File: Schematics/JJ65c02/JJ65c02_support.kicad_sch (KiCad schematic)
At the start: 37 parts, among them J1 AudioJack, SW2 SW_SPDT, U10 VIA Port Shifter, U11 Misc Shifter, U5 TLV2217-33KCSE3, U9 Data Level Shifter, X1 4Mhz, X2 1.8Mhz

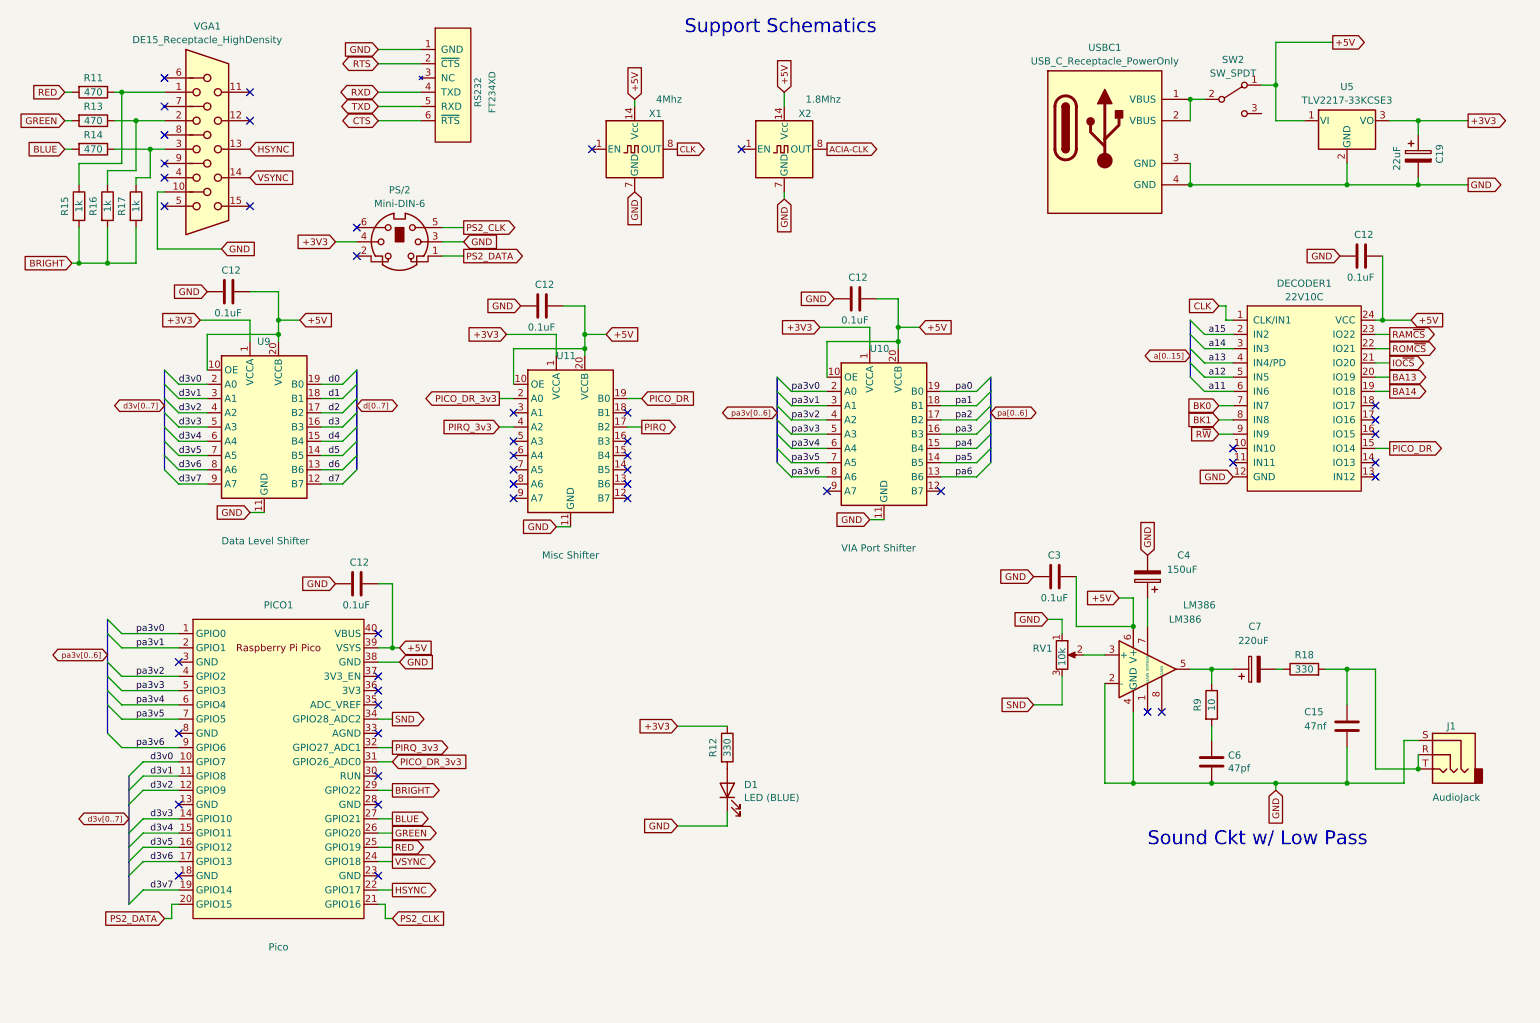
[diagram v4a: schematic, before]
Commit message: Updated schematics for v2-pico
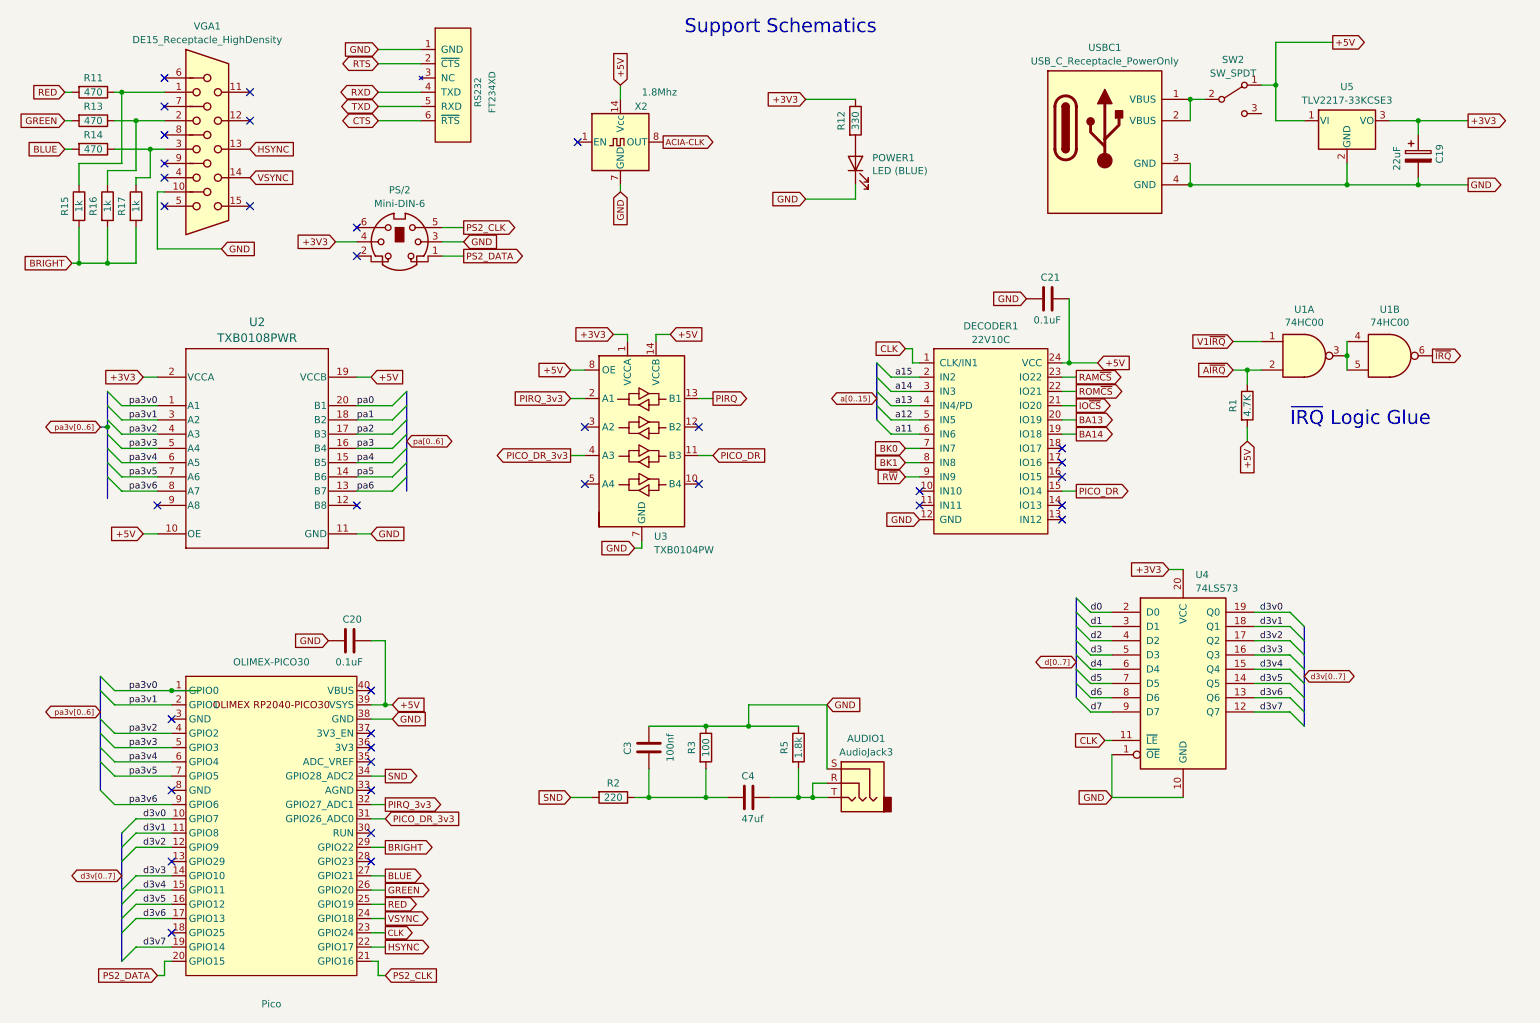
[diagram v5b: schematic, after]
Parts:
- removed C12 (x3): 0.1uF, Capacitor_THT:C_Disc_D4.7mm_W2.5mm_P5.00mm, symbol Device:C
- removed C15: 47nf, Capacitor_THT:C_Disc_D4.7mm_W2.5mm_P5.00mm, symbol Device:C
- removed C4: 150uF, Capacitor_THT:CP_Radial_D5.0mm_P2.50mm, symbol Device:C_Polarized
- removed C6: 47pf, Capacitor_THT:C_Disc_D4.7mm_W2.5mm_P5.00mm, symbol Device:C
- removed C7: 220uF, Capacitor_THT:CP_Radial_D6.3mm_P2.50mm, symbol Device:C_Polarized
- removed J1: AudioJack, Connector_Audio:Jack_3.5mm_CUI_SJ1-3533NG_Horizontal, symbol Connector:AudioJack3
- removed LM386: LM386, Package_DIP:DIP-8_W7.62mm_Socket, symbol Amplifier_Audio:LM386
- removed R18: 330, Resistor_THT:R_Axial_DIN0207_L6.3mm_D2.5mm_P7.62mm_Horizontal, symbol Device:R
- removed R9: 10, Resistor_THT:R_Axial_DIN0207_L6.3mm_D2.5mm_P7.62mm_Horizontal, symbol Device:R
- removed RV1: 10k, Potentiometer_THT:Potentiometer_Bourns_3339P_Vertical, symbol Device:R_Potentiometer
- removed U10: VIA Port Shifter, JJ65c02:TXB0108, symbol JJ65c02-rescue:FXMA108
- removed U11: Misc Shifter, JJ65c02:TXB0108, symbol JJ65c02-rescue:FXMA108
- removed U9: Data Level Shifter, JJ65c02:TXB0108, symbol JJ65c02-rescue:FXMA108
- removed X1: 4Mhz, Oscillator:Oscillator_DIP-14, symbol Oscillator:CXO_DIP14
- added AUDIO1: AudioJack3, Connector_Audio:Jack_3.5mm_CUI_SJ1-3533NG_Horizontal, symbol Connector_Audio:AudioJack3
- added C4: 47uf, Capacitor_THT:C_Disc_D4.7mm_W2.5mm_P5.00mm, symbol Device:C
- added R1: 4.7K, Resistor_THT:R_Axial_DIN0207_L6.3mm_D2.5mm_P7.62mm_Horizontal, symbol Device:R
- added R2: 220, Resistor_THT:R_Axial_DIN0207_L6.3mm_D2.5mm_P7.62mm_Horizontal, symbol Device:R
- added R3: 100, Resistor_THT:R_Axial_DIN0207_L6.3mm_D2.5mm_P7.62mm_Horizontal, symbol Device:R
- added R5: 1.8k, Resistor_THT:R_Axial_DIN0207_L6.3mm_D2.5mm_P7.62mm_Horizontal, symbol Device:R
- added U1: 74HC00, Package_DIP:DIP-14_W7.62mm_Socket, symbol 74xx:74HC00
- added U2: TXB0108PWR, Package_SO:TSSOP-20_4.4x6.5mm_P0.65mm, symbol 2024-01-03_21-33-35:TXB0108PWR
- added U3: TXB0104PW, Package_SO:SOIC-14_3.9x8.7mm_P1.27mm, symbol Logic_LevelTranslator:TXB0104PW
- added U4: 74LS573, Package_SO:SOIC-20W_7.5x12.8mm_P1.27mm, symbol 74xx:74LS573
- C3: value 0.1uF -> 100nf
- renumbered C12 to C20, C12 to C21, PICO1 to OLIMEX-PICO30, D1 to POWER1
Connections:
- net +3V3: now also U2.2 (VCCA), U3.1 (VCCA), U4.20 (VCC)
- net +5V: now also R1.2, U2.10 (OE), U2.19 (VCCB), U3.14 (VCCB), U3.8 (OE); no longer C3.1
- net CLK: now also OLIMEX-PICO30.23 (GPIO24), U4.11 (~{LE})
- net GND: now also C3.1, AUDIO1.S, R3.1, R5.1, U2.11 (GND), U3.7 (GND), U4.1 (~{OE}), U4.10 (GND); no longer C3.2
- net PICO_DR: now also U3.11 (B3)
- net PICO_DR_3v3: now also U3.4 (A3)
- net PIRQ: now also U3.13 (B1)
- net PIRQ_3v3: now also U3.2 (A1)
- net SND: now also R2.2
- net d0: now also U4.2 (D0)
- net d1: now also U4.3 (D1)
- net d2: now also U4.4 (D2)
- net d3: now also U4.5 (D3)
- net d3v0: now also U4.19 (Q0)
- net d3v1: now also U4.18 (Q1)
- net d3v2: now also U4.17 (Q2)
- net d3v3: now also U4.16 (Q3)
- net d3v4: now also U4.15 (Q4)
- net d3v5: now also U4.14 (Q5)
- net d3v6: now also U4.13 (Q6)
- net d3v7: now also U4.12 (Q7)
- net d4: now also U4.6 (D4)
- net d5: now also U4.7 (D5)
- net d6: now also U4.8 (D6)
- net d7: now also U4.9 (D7)
- net pa0: now also U2.20 (B1)
- net pa1: now also U2.18 (B2)
- net pa2: now also U2.17 (B3)
- net pa3: now also U2.16 (B4)
- net pa3v0: now also U2.1 (A1)
- net pa3v1: now also U2.3 (A2)
- net pa3v2: now also U2.4 (A3)
- net pa3v3: now also U2.5 (A4)
- net pa3v4: now also U2.6 (A5)
- net pa3v5: now also U2.7 (A6)
- net pa3v6: now also U2.8 (A7)
- net pa4: now also U2.15 (B5)
- net pa5: now also U2.14 (B6)
- net pa6: now also U2.13 (B7)
- new net: C3.2, C4.2, R2.1, R3.2
- new net: U1.3, U1.4, U1.5
- new net: AUDIO1.R, AUDIO1.T, C4.1, R5.2
- new net A~{IRQ}: R1.1, U1.2
- new net V1~{IRQ}: U1.1
- new net ~{IRQ}: U1.6
- no-connect marks 48 -> 36
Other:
- note added: "~{IRQ} Logic Glue"
- note removed: "Sound Ckt w/ Low Pass"
- moved on the sheet: C20, C21, DECODER1, OLIMEX-PICO30, POWER1, R12, X2

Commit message: if we are using the pi pico to generate the clock, we need to level convert from 3.3 to 5v
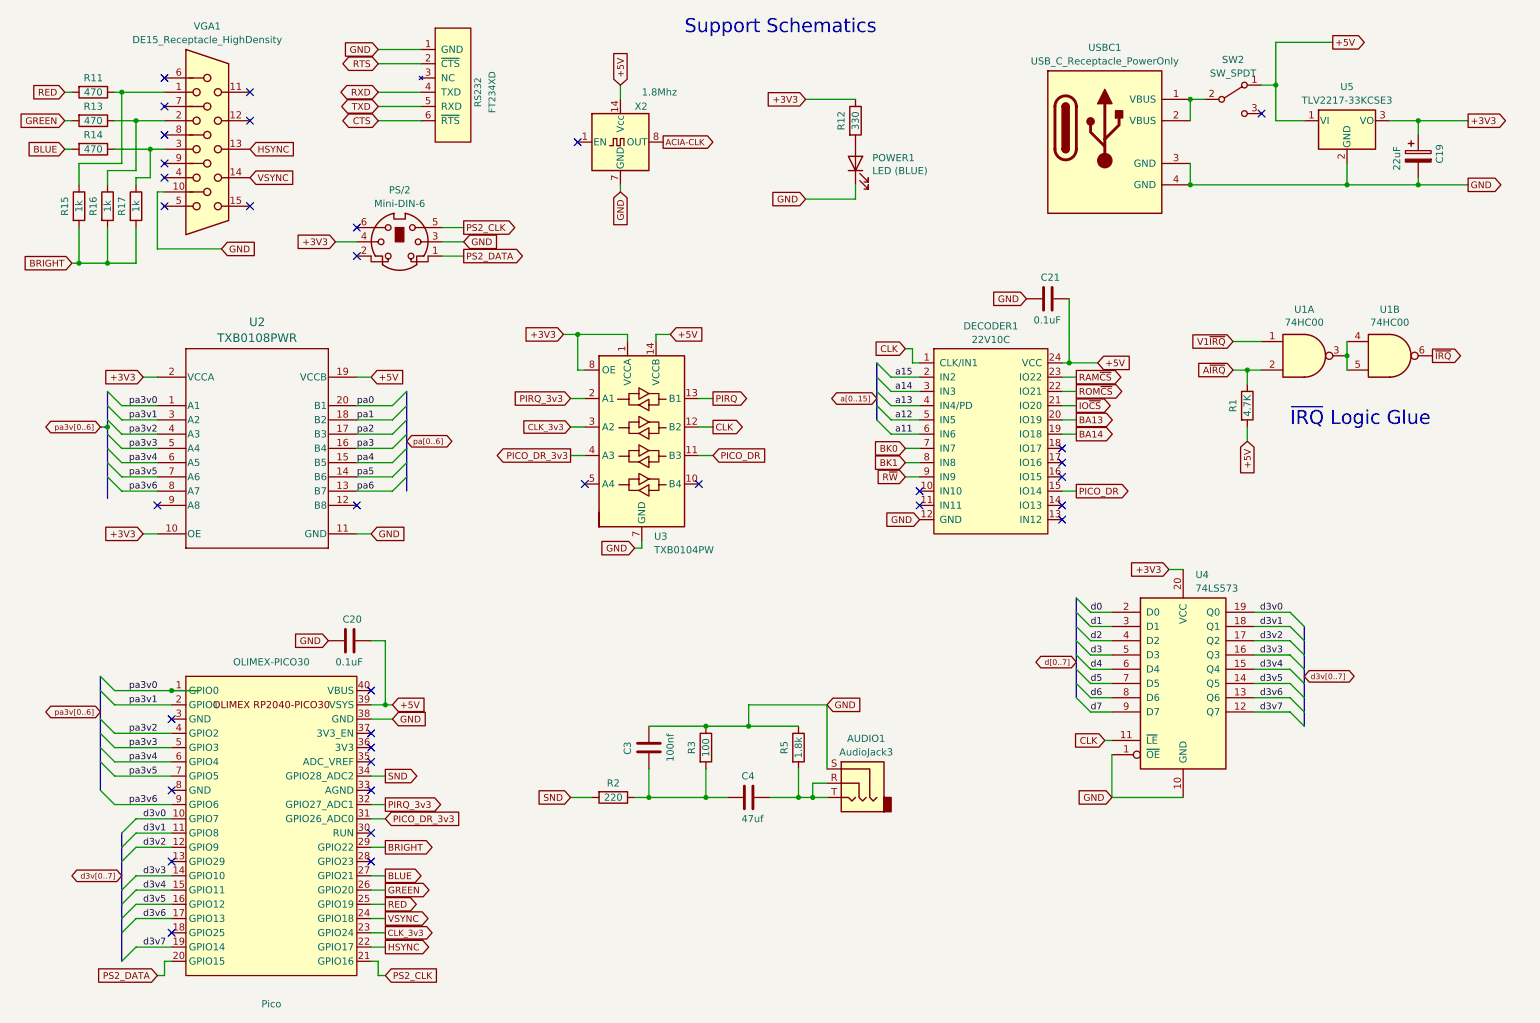
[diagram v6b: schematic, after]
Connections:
- net +3V3: now also U2.10 (OE), U3.8 (OE)
- net +5V: no longer U2.10 (OE), U3.8 (OE)
- net CLK: now also U3.12 (B2); no longer OLIMEX-PICO30.23 (GPIO24)
- net CLK_3v3: now reaches U3.3 (A2)
- net CLK_3v3: now also OLIMEX-PICO30.23 (GPIO24)
- no-connect marks 36 -> 35
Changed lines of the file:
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@@
   (junction (at 143.51 140.97) (diameter 0) (color 0 0 0 0)
+  )
+  (junction (at 113.03 71.12) (diameter 0) (color 0 0 0 0)
   )
   (junction (at 152.4 153.67) (diameter 0) (color 0 0 0 0)
@@
   (no_connect (at 39.37 40.64))
   (no_connect (at 173.99 99.06))
+  (no_connect (at 234.95 31.75))
   (no_connect (at 76.2 165.1))
   (no_connect (at 40.64 152.4))
@@
   (no_connect (at 76.2 142.24))
   (no_connect (at 173.99 101.6))
-  (no_connect (at 114.3 87.63))
   (no_connect (at 199.39 91.44))
-  (no_connect (at 134.62 87.63))
   (no_connect (at 39.37 35.56))
   (bus_entry (at 27.94 144.78) (size 2.54 2.54)
@@
     (stroke (width 0) (type default))
   )
+  (wire (pts (xy 113.03 71.12) (xy 113.03 77.47))
+    (stroke (width 0) (type default))
+  )
   (bus (pts (xy 29.21 93.98) (xy 29.21 96.52))
     (stroke (width 0) (type default))
@@
     (stroke (width 0) (type default))
   )
+  (wire (pts (xy 134.62 87.63) (xy 137.16 87.63))
+    (stroke (width 0) (type default))
+  )
   (bus (pts (xy 31.75 177.8) (xy 31.75 182.88))
     (stroke (width 0) (type default))
@@
     (stroke (width 0) (type default))
   )
+  (wire (pts (xy 111.76 87.63) (xy 114.3 87.63))
+    (stroke (width 0) (type default))
+  )
   (bus (pts (xy 27.94 144.78) (xy 27.94 147.32))
     (stroke (width 0) (type default))
@@
     (stroke (width 0) (type default))
   )
+  (wire (pts (xy 113.03 77.47) (xy 114.3 77.47))
+    (stroke (width 0) (type default))
+  )
   (bus (pts (xy 29.21 83.82) (xy 29.21 86.36))
     (stroke (width 0) (type default))
@@
     (stroke (width 0) (type default))
   )
-  (wire (pts (xy 111.76 77.47) (xy 114.3 77.47))
-    (stroke (width 0) (type default))
-  )
   (wire (pts (xy 31.75 40.64) (xy 31.75 27.94))
     (stroke (width 0) (type default))
@@
     (stroke (width 0) (type default))
   )
+  (wire (pts (xy 113.03 71.12) (xy 121.92 71.12))
+    (stroke (width 0) (type default))
+  )
   (wire (pts (xy 233.68 128.27) (xy 240.03 128.27))
     (stroke (width 0) (type default))
@@
     (stroke (width 0) (type default))
   )
-  (wire (pts (xy 119.38 71.12) (xy 121.92 71.12))
+  (wire (pts (xy 110.49 71.12) (xy 113.03 71.12))
     (stroke (width 0) (type default))
   )
@@
     )
   )
-  (global_label "+5V" (shape input) (at 111.76 77.47 180) (fields_autoplaced)
-    (effects (font (size 1.1938 1.1938)) (justify right))
-    (property "Intersheetrefs" "${INTERSHEET_REFS}" (at 105.9308 77.47 0)
-      (effects (font (size 1.27 1.27)) (justify right) hide)
-    )
-  )
   (global_label "GND" (shape input) (at 77.47 20.32 180) (fields_autoplaced)
     (effects (font (size 1.1938 1.1938)) (justify right))
@@
     )
   )
-  (global_label "+3V3" (shape input) (at 119.38 71.12 180) (fields_autoplaced)
-    (effects (font (size 1.1938 1.1938)) (justify right))
-    (property "Intersheetrefs" "${INTERSHEET_REFS}" (at 112.4138 71.12 0)
+  (global_label "+3V3" (shape input) (at 110.49 71.12 180) (fields_autoplaced)
+    (effects (font (size 1.1938 1.1938)) (justify right))
+    (property "Intersheetrefs" "${INTERSHEET_REFS}" (at 103.5238 71.12 0)
       (effects (font (size 1.1938 1.1938)) (justify right) hide)
     )
@@
     )
   )
+  (global_label "+3V3" (shape input) (at 35.56 106.68 180) (fields_autoplaced)
+    (effects (font (size 1.1938 1.1938)) (justify right))
+    (property "Intersheetrefs" "${INTERSHEET_REFS}" (at 28.5938 106.68 0)
+      (effects (font (size 1.1938 1.1938)) (justify right) hide)
+    )
+  )
   (global_label "GND" (shape input) (at 153.67 46.99 180) (fields_autoplaced)
     (effects (font (size 1.1938 1.1938)) (justify right))
@@
     )
   )
-  (global_label "CLK" (shape output) (at 78.74 177.8 0) (fields_autoplaced)
+  (global_label "CLK_3v3" (shape output) (at 78.74 177.8 0) (fields_autoplaced)
     (effects (font (size 1.0922 1.0922)) (justify left))
-    (property "Intersheetrefs" "${INTERSHEET_REFS}" (at -153.67 116.84 0)
-      (effects (font (size 1.27 1.27)) hide)
+    (property "Intersheetrefs" "${INTERSHEET_REFS}" (at 87.558 177.8 0)
+      (effects (font (size 1.27 1.27)) (justify left) hide)
     )
   )
@@
     (property "Intersheetrefs" "${INTERSHEET_REFS}" (at 88.6623 185.42 0)
       (effects (font (size 1.27 1.27)) (justify left) hide)
+    )
+  )
+  (global_label "CLK_3v3" (shape input) (at 111.76 87.63 180) (fields_autoplaced)
+    (effects (font (size 1.0922 1.0922)) (justify right))
+    (property "Intersheetrefs" "${INTERSHEET_REFS}" (at 102.942 87.63 0)
+      (effects (font (size 1.27 1.27)) (justify right) hide)
     )
   )
@@
     )
   )
+  (global_label "CLK" (shape output) (at 137.16 87.63 0) (fields_autoplaced)
+    (effects (font (size 1.1938 1.1938)) (justify left))
+    (property "Intersheetrefs" "${INTERSHEET_REFS}" (at 142.7049 87.63 0)
+      (effects (font (size 1.27 1.27)) (justify left) hide)
+    )
+  )
   (global_label "+5V" (shape input) (at 205.74 76.2 0) (fields_autoplaced)
     (effects (font (size 1.1938 1.1938)) (justify left))
@@
     )
   )
-  (global_label "+5V" (shape input) (at 35.56 106.68 180) (fields_autoplaced)
-    (effects (font (size 1.1938 1.1938)) (justify right))
-    (property "Intersheetrefs" "${INTERSHEET_REFS}" (at 29.7308 106.68 0)
-      (effects (font (size 1.27 1.27)) (justify right) hide)
-    )
-  )
